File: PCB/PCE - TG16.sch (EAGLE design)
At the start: 13 parts, among them U1 SN74AHCT125N, U2 SN74AHCT125N

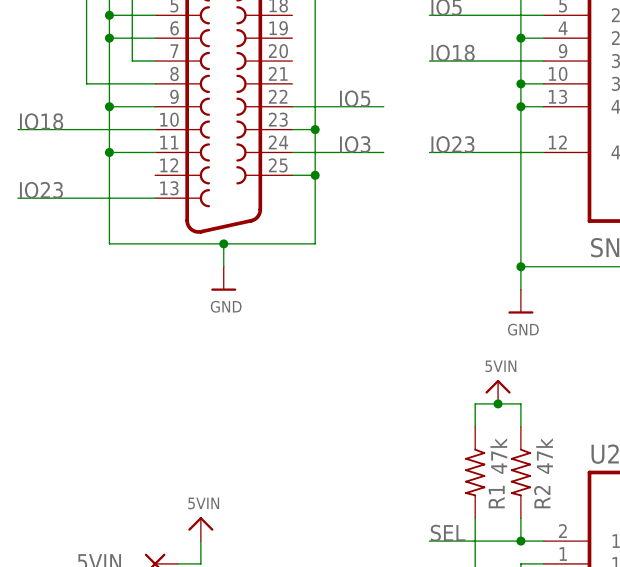
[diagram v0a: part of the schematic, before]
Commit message: Added exposed GND plane at DB25 anchors
All PCBs have been update to have exposed GND plane pads for the DB25 anchor points.

This resolves Issue 54
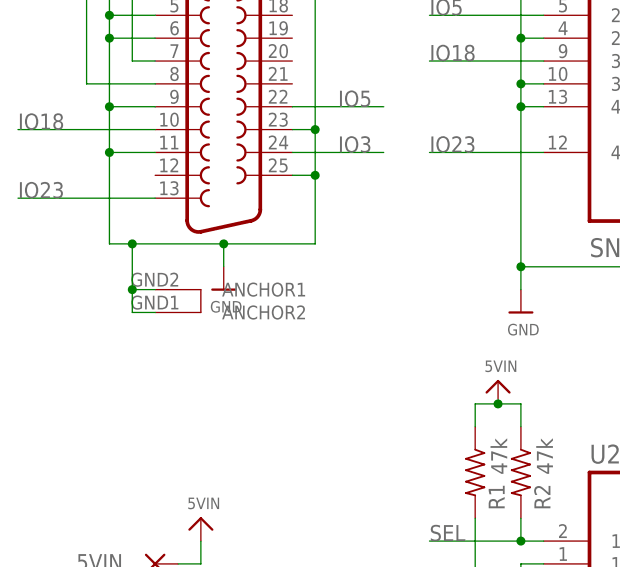
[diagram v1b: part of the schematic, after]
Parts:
- X1: device SparkFun-Retired:DB25_FEMALEH -> SparkFun-Retired:DB25_FEMALEHP
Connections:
- net GND: now also X1.ANCHOR1, X1.ANCHOR2
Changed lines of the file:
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@@
 </classes>
 <parts>
-<part name="X1" library="SparkFun-Retired" deviceset="DB25_FEMALE" device="H"/>
+<part name="X1" library="SparkFun-Retired" deviceset="DB25_FEMALE" device="HP"/>
 <part name="U$43" library="microbuilder" deviceset="VIN" device="" value="3V3IN"/>
 <part name="U$44" library="microbuilder" deviceset="VIN" device="" value="5VIN"/>
@@
 <segment>
 <wire x1="248.92" y1="-109.22" x2="238.76" y2="-109.22" width="0.1524" layer="91"/>
-<wire x1="238.76" y1="-109.22" x2="226.06" y2="-109.22" width="0.1524" layer="91"/>
+<wire x1="238.76" y1="-109.22" x2="228.6" y2="-109.22" width="0.1524" layer="91"/>
+<wire x1="228.6" y1="-109.22" x2="226.06" y2="-109.22" width="0.1524" layer="91"/>
 <wire x1="238.76" y1="-109.22" x2="238.76" y2="-111.76" width="0.1524" layer="91"/>
 <junction x="238.76" y="-109.22"/>
@@
 <wire x1="226.06" y1="-76.2" x2="226.06" y2="-78.74" width="0.1524" layer="91"/>
 <junction x="226.06" y="-78.74"/>
+<pinref part="X1" gate="-1" pin="ANCHOR2"/>
+<wire x1="231.14" y1="-116.84" x2="228.6" y2="-116.84" width="0.1524" layer="91"/>
+<wire x1="228.6" y1="-116.84" x2="228.6" y2="-114.3" width="0.1524" layer="91"/>
+<junction x="228.6" y="-109.22"/>
+<pinref part="X1" gate="-1" pin="ANCHOR1"/>
+<wire x1="228.6" y1="-114.3" x2="228.6" y2="-109.22" width="0.1524" layer="91"/>
+<wire x1="231.14" y1="-114.3" x2="228.6" y2="-114.3" width="0.1524" layer="91"/>
+<junction x="228.6" y="-114.3"/>
 </segment>
 <segment>
